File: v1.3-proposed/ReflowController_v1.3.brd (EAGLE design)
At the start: 95.2 x 50.8 mm, 52 parts, among them J1 AVR_SPI_PRG_62X3_LOCK

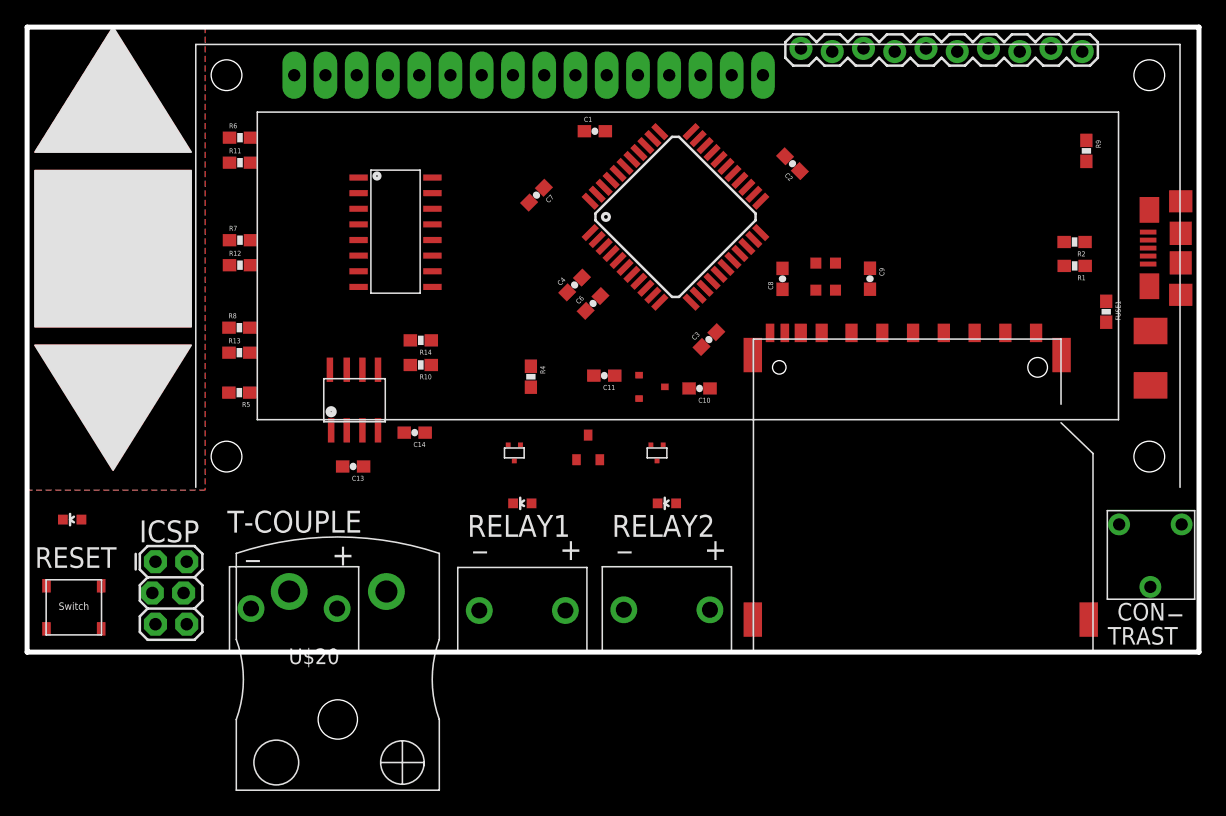
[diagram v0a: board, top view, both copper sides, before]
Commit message: Added 2 servo interfaces, many pin swaps
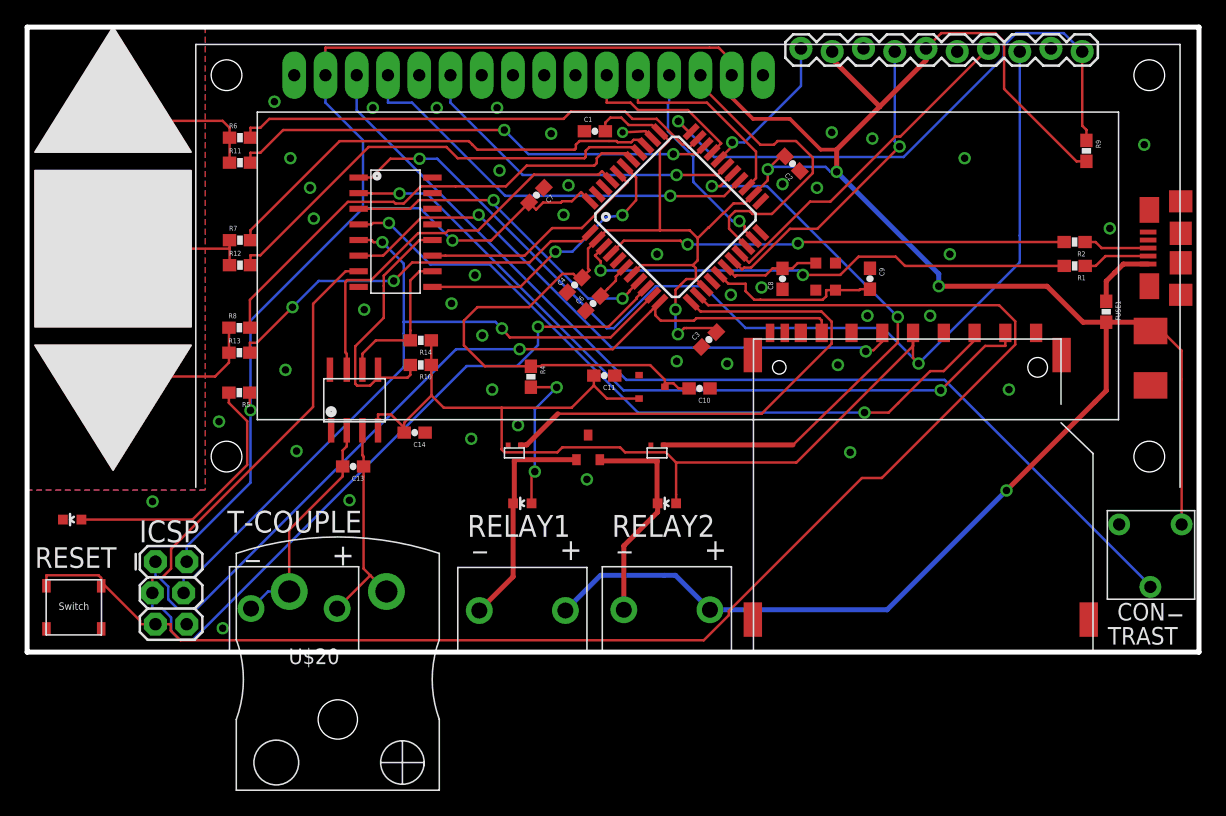
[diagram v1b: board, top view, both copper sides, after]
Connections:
- net D0: now also JP3.4; no longer U$16.GATE
- net D7: now also U$16.GATE; no longer JP3.4
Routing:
- net 5V: track 0.00 -> 362.2 mm, vias 0 -> 8
- net 3.3V: track 0.00 -> 164.8 mm, vias 0 -> 2
- net RESET: track 0.00 -> 121.5 mm
- net SCK: track 0.00 -> 90.0 mm, vias 0 -> 1
- net TRIM: track 0.00 -> 83.5 mm
- net MISO: track 0.00 -> 69.8 mm, vias 0 -> 1
- net SS-L: track 0.00 -> 61.8 mm, vias 0 -> 2
- net MOSI: track 0.00 -> 61.3 mm, vias 0 -> 2
- net MOSI-L: track 0.00 -> 59.5 mm, vias 0 -> 2
- net SCK-L: track 0.00 -> 49.6 mm, vias 0 -> 2
- net HWB: track 0.00 -> 48.1 mm, vias 0 -> 1
- net D7: track 0.00 -> 46.2 mm, vias 0 -> 2
- net B7: track 0.00 -> 42.6 mm
- net N$7: track 0.00 -> 41.2 mm, vias 0 -> 2
- net UPSENSE: track 0.00 -> 39.7 mm, vias 0 -> 2
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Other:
- board text added: "~3"
- board text removed: "~6"

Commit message: Added 2 servo interfaces, many pin swaps
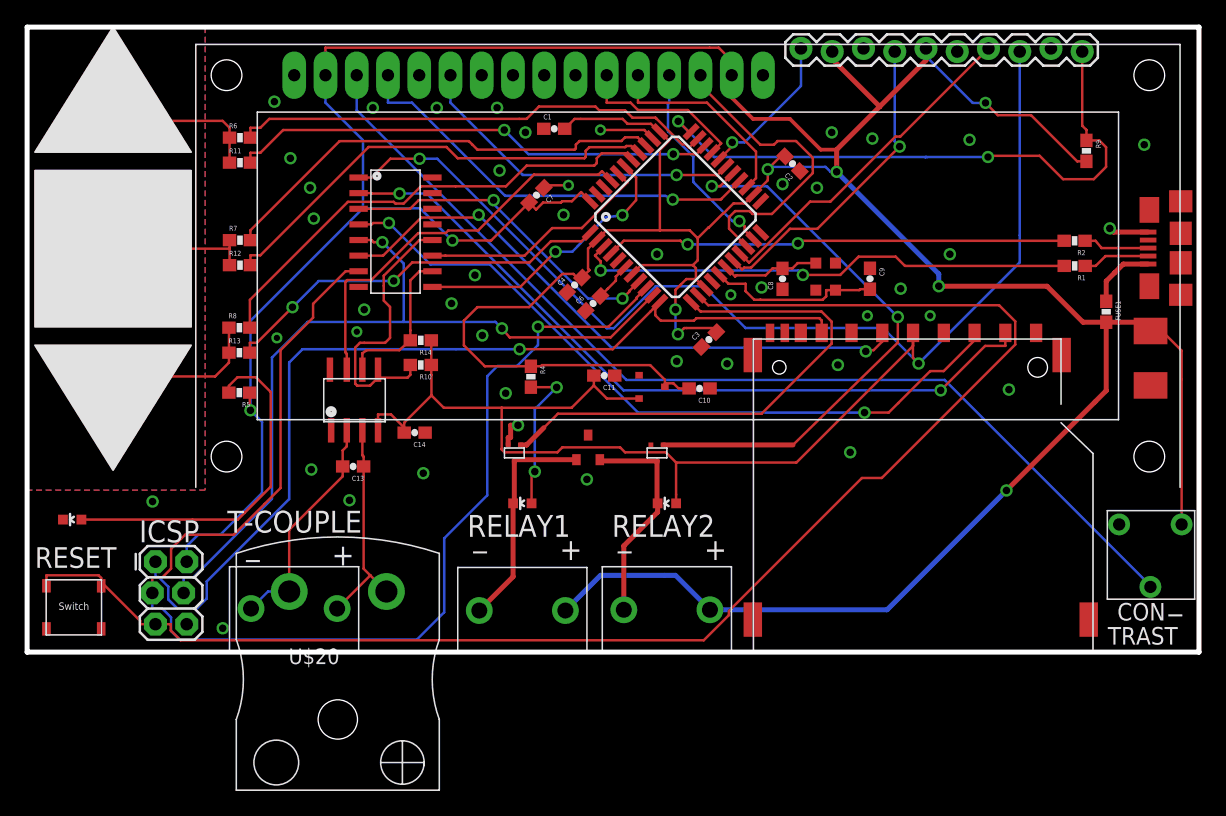
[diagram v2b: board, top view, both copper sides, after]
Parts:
- moved C1 3.31 mm to (42.8, 52.7)
- moved R2 0.10 mm to (85.1, 43.6)
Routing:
- net SCK: track 90.0 -> 101.5 mm
- net GND: track 2.72 -> 12.3 mm, vias 44 -> 45
- net MISO: track 69.8 -> 77.1 mm
- net N$4: track 21.8 -> 28.9 mm
- net MOSI: track 61.3 -> 65.9 mm
- net 5V: track 362.2 -> 363.8 mm, vias 8 -> 9
- net TC-SCK-L: track 21.3 -> 22.9 mm
- net HWB: track 48.1 -> 49.6 mm, vias 1 -> 2

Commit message: Added 2 servo interfaces, many pin swaps
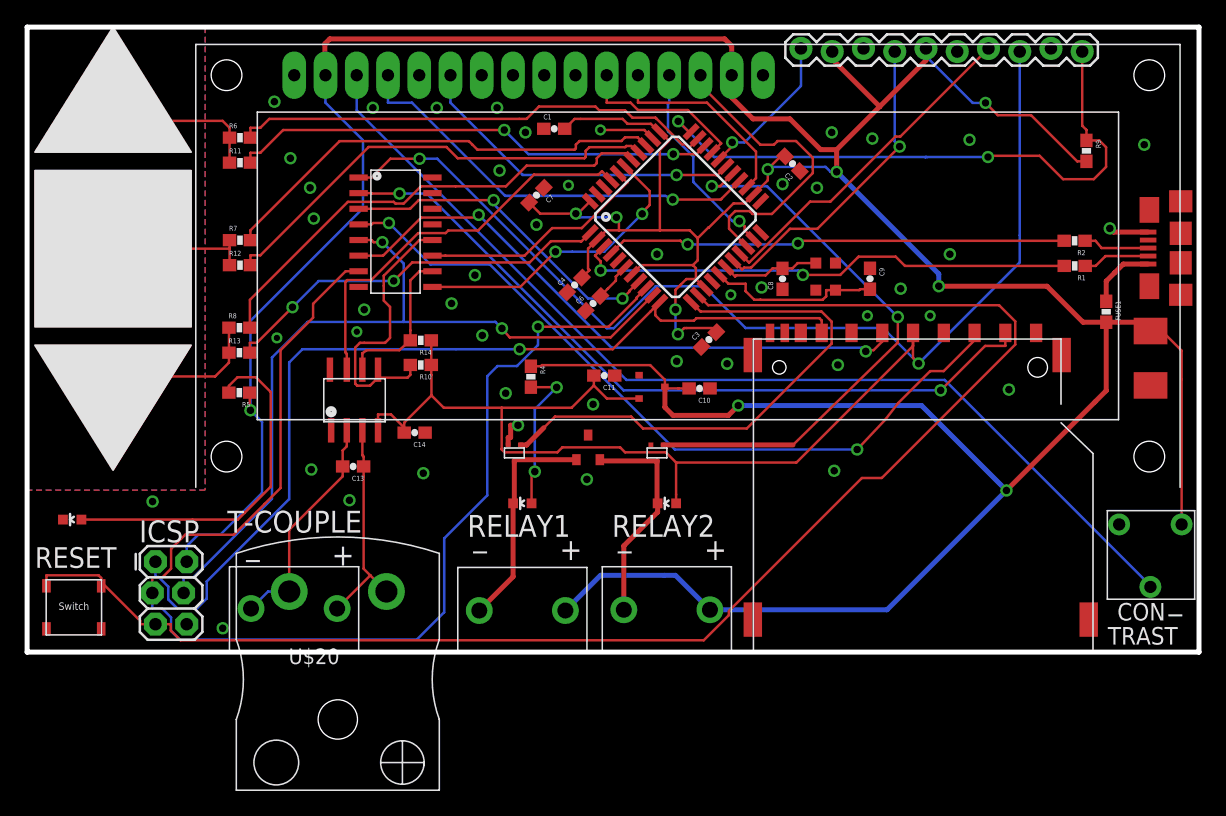
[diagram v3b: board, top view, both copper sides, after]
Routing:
- net 5V: track 363.8 -> 367.7 mm, vias 9 -> 11
- net MOSI-L: track 59.5 -> 62.2 mm
- net F4: track 22.6 -> 24.4 mm
- net GND: track 12.3 -> 10.5 mm, vias 45 -> 46
- net B7: track 42.6 -> 43.4 mm

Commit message: Added 2 servo interfaces, many optimizations
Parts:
- added R3: 390, SparkFun-Passives:0603-RES
- R4: value 150 -> 680
- R5: value 150 -> 510
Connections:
- new net N$6: LED3.A, R3.2
- net 3.3V: no longer LED3.A
- net 5V: now also R3.1
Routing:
- net 3.3V: track 164.8 -> 137.8 mm, vias 2 -> 3
- net 5V: track 367.7 -> 379.4 mm
- net N$6: track 0.00 -> 2.65 mm
- net GND: vias 46 -> 48
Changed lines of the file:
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@@
 <attribute name="VALUE" x="4.6785" y="22.0108" size="0.4064" layer="27" rot="R180"/>
 </element>
-<element name="R4" library="SparkFun-Passives" package="0603-RES" value="150" x="40.9472" y="32.5431" rot="R270"/>
-<element name="R5" library="SparkFun-Passives" package="0603-RES" value="150" x="17.25" y="31.25" rot="R180"/>
+<element name="R4" library="SparkFun-Passives" package="0603-RES" value="680" x="40.9472" y="32.5431" rot="R270"/>
+<element name="R5" library="SparkFun-Passives" package="0603-RES" value="510" x="17.25" y="31.25" rot="R180"/>
 <element name="U$13" library="JKCustom" package="CAPTOUCH_ARROW" value="CAPTOUCH_ARROW" x="6.985" y="50.8"/>
 <element name="U$14" library="JKCustom" package="CAPTOUCH_ARROW" value="CAPTOUCH_ARROW" x="6.985" y="35.1028" rot="R180"/>
@@
 <element name="JP3" library="SparkFun-Connectors" package="1X10_LOCK" value="M10LOCK" x="62.9" y="59.1" smashed="yes"/>
 <element name="R9" library="SparkFun-Passives" package="0603-RES" value="10K" x="86.1" y="50.9" rot="R270"/>
+<element name="R3" library="SparkFun-Passives" package="0603-RES" value="390" x="53.6" y="24.9" rot="R180"/>
 </elements>
 <signals>
@@
 <via x="59.7" y="39.8" extent="1-16" drill="0.609596875" diameter="1.016"/>
 <via x="76.6" y="51.8" extent="1-16" drill="0.609596875" diameter="1.016"/>
-<via x="65.6" y="24.9" extent="1-16" drill="0.609596875" diameter="1.016"/>
+<via x="62.7" y="22.5" extent="1-16" drill="0.609596875" diameter="1.016"/>
 <via x="90.8" y="51.4" extent="1-16" drill="0.609596875" diameter="1.016"/>
 <via x="71" y="39.7" extent="1-16" drill="0.609596875" diameter="1.016"/>
@@
 <via x="57.2" y="39.2" extent="1-16" drill="0.508" diameter="0.762"/>
 <via x="52.8" y="33.8" extent="1-16" drill="0.609596875" diameter="1.016"/>
-<via x="38.9" y="31.2" extent="1-16" drill="0.609596875" diameter="1.016"/>
+<via x="35.9" y="32.2" extent="1-16" drill="0.609596875" diameter="1.016"/>
 <via x="45.5" y="24.2" extent="1-16" drill="0.609596875" diameter="1.016"/>
 <via x="51.2" y="42.5" extent="1-16" drill="0.609596875" diameter="1.016"/>
@@
 <wire x1="39.3" y1="28.6" x2="39.9" y2="28.6" width="0.4064" layer="1"/>
 <via x="46" y="30.3" extent="1-16" drill="0.609596875" diameter="1.016"/>
+<via x="47.6" y="28.2" extent="1-16" drill="0.609596875" diameter="1.016"/>
+<via x="43.6" y="28.2" extent="1-16" drill="0.609596875" diameter="1.016"/>
 </signal>
 <signal name="5V">
@@
 <wire x1="40.80065625" y1="46.69955625" x2="41.7002125" y2="45.8" width="0.2032" layer="1"/>
 <wire x1="41.7002125" y1="45.8" x2="44.6" y2="45.8" width="0.2032" layer="1"/>
+<contactref element="R3" pad="1"/>
+<wire x1="54.45" y1="24.9" x2="55.5" y2="23.95" width="0.2032" layer="1"/>
+<wire x1="55.5" y1="23.95" x2="55.5" y2="13.6" width="0.2032" layer="1"/>
 <wire x1="61.6069" y1="50.4598" x2="61.60685625" y2="50.459840625" width="0" layer="19" extent="1-1"/>
 <wire x1="59.065959375" y1="47.372175" x2="59.066" y2="47.3722" width="0" layer="19" extent="1-1"/>
@@
 <contactref element="U$1" pad="8"/>
 <contactref element="U$8" pad="P$3"/>
-<wire x1="37.9142" y1="46.8963" x2="37.9142" y2="46.5858" width="0.2032" layer="16"/>
-<wire x1="37.9142" y1="46.5858" x2="45.5978" y2="38.9022" width="0.2032" layer="16"/>
 <wire x1="45.5978" y1="38.9022" x2="48.3917" y2="38.9022" width="0.2032" layer="16"/>
 <wire x1="27.9989" y1="46.194" x2="31.1303" y2="46.194" width="0.2032" layer="1"/>
@@
 <via x="48.3917" y="38.9022" extent="1-16" drill="0.609596875" diameter="1.016"/>
 <via x="37.9142" y="46.8963" extent="1-16" drill="0.609596875" diameter="1.016"/>
+<wire x1="45.5978" y1="38.9022" x2="44" y2="40.5" width="0.2032" layer="16"/>
+<wire x1="44" y1="40.5" x2="44" y2="41.1" width="0.2032" layer="16"/>
+<wire x1="44" y1="41.1" x2="43.4" y2="41.7" width="0.2032" layer="16"/>
+<wire x1="43.4" y1="41.7" x2="42.7" y2="41.7" width="0.2032" layer="16"/>
+<wire x1="37.9142" y1="46.8963" x2="38.1142" y2="46.2858" width="0.2032" layer="16"/>
+<wire x1="38.1142" y1="46.2858" x2="42.7" y2="41.7" width="0.2032" layer="16"/>
 <wire x1="49.7322" y1="40.3011" x2="49.73215" y2="40.301109375" width="0" layer="19" extent="1-1"/>
 </signal>
@@
 <contactref element="C14" pad="2"/>
 <contactref element="R14" pad="1"/>
-<contactref element="LED3" pad="A"/>
 <contactref element="R10" pad="1"/>
 <contactref element="JP3" pad="8"/>
 <wire x1="27.9989" y1="48.734" x2="29.5268" y2="50.2619" width="0.2032" layer="1"/>
 <wire x1="29.5268" y1="50.2619" x2="31.8966" y2="50.2619" width="0.2032" layer="1"/>
-<wire x1="47.1135" y1="36.4833" x2="33.335" y2="50.2618" width="0.2032" layer="16"/>
-<wire x1="33.335" y1="50.2618" x2="31.8966" y2="50.2618" width="0.2032" layer="16"/>
 <wire x1="31.8966" y1="50.2618" x2="31.8966" y2="50.2619" width="0.2032" layer="16"/>
-<wire x1="52.75" y1="25.5696" x2="52.75" y2="22.9549" width="0.2032" layer="1"/>
-<wire x1="72.0103" y1="35.0497" x2="62.5302" y2="25.5696" width="0.2032" layer="1"/>
-<wire x1="62.5302" y1="25.5696" x2="52.75" y2="25.5696" width="0.2032" layer="1"/>
+<wire x1="72.0103" y1="35.0497" x2="63.1302" y2="26.0696" width="0.2032" layer="1"/>
+<wire x1="63.1302" y1="26.0696" x2="52.35" y2="26.0696" width="0.2032" layer="1"/>
 <wire x1="38.572" y1="26.6851" x2="38.572" y2="30.0218" width="0.2032" layer="1"/>
 <wire x1="38.572" y1="30.0218" x2="33.8663" y2="30.0218" width="0.2032" layer="1"/>
@@
 <wire x1="32.85" y1="33.5" x2="32.85" y2="32.6951" width="0.2032" layer="1"/>
 <wire x1="32.85" y1="33.5" x2="32.85" y2="35.5" width="0.2032" layer="1"/>
-<wire x1="52.75" y1="22.25" x2="52.75" y2="22.9549" width="0.2032" layer="1"/>
 <wire x1="72.0103" y1="36.1046" x2="72.0103" y2="35.0497" width="0.2032" layer="1"/>
 <via x="72.4603" y="33.6165" extent="1-16" drill="0.609596875" diameter="1.016"/>
-<wire x1="47.1135" y1="36.4833" x2="47.6833" y2="36.4833" width="0.2032" layer="16"/>
-<wire x1="47.6833" y1="36.4833" x2="51.1" y2="39.9" width="0.2032" layer="16"/>
-<wire x1="51.1" y1="39.9" x2="55" y2="39.9" width="0.2032" layer="16"/>
-<wire x1="55" y1="39.9" x2="58.4" y2="36.5" width="0.2032" layer="16"/>
-<wire x1="58.4" y1="36.5" x2="69.0438" y2="36.5" width="0.2032" layer="16"/>
-<wire x1="70.4438" y1="35.633" x2="72.4603" y2="33.6165" width="0.2032" layer="16"/>
 <wire x1="72.0103" y1="36.1046" x2="72" y2="36.1046" width="0.2032" layer="1"/>
 <wire x1="72" y1="36.1046" x2="72" y2="35" width="0.2032" layer="1"/>
@@
 <wire x1="80.68" y1="44.0362" x2="80.68" y2="41.8362" width="0.2032" layer="16"/>
 <wire x1="80.68" y1="41.8362" x2="72.4603" y2="33.6165" width="0.2032" layer="16"/>
-<wire x1="70.4438" y1="35.633" x2="69.5768" y2="36.5" width="0.2032" layer="16"/>
-<wire x1="69.5768" y1="36.5" x2="69.0438" y2="36.5" width="0.2032" layer="16"/>
 <wire x1="38.572" y1="26.6851" x2="38.572" y2="26.628" width="0.2032" layer="1"/>
 <wire x1="38.572" y1="26.628" x2="38.8" y2="26.4" width="0.2032" layer="1"/>
@@
 <wire x1="48.2" y1="26.8" x2="48.6" y2="26.4" width="0.2032" layer="1"/>
 <wire x1="48.6" y1="26.4" x2="51.9196" y2="26.4" width="0.2032" layer="1"/>
-<wire x1="51.9196" y1="26.4" x2="52.75" y2="25.5696" width="0.2032" layer="1"/>
+<wire x1="51.9196" y1="26.4" x2="52.35" y2="26.0696" width="0.2032" layer="1"/>
+<wire x1="31.8966" y1="50.2618" x2="33.3382" y2="50.2618" width="0.2032" layer="16"/>
+<wire x1="33.3382" y1="50.2618" x2="42.8" y2="40.8" width="0.2032" layer="16"/>
+<via x="42.8" y="40.8" extent="1-16" drill="0.6"/>
+<wire x1="42.8" y1="40.8" x2="40.1" y2="38.1" width="0.2032" layer="1"/>
+<wire x1="40.1" y1="38.1" x2="36.4" y2="38.1" width="0.2032" layer="1"/>
+<wire x1="36.4" y1="38.1" x2="33.8" y2="35.5" width="0.2032" layer="1"/>
+<wire x1="33.8" y1="35.5" x2="32.85" y2="35.5" width="0.2032" layer="1"/>
 </signal>
 <signal name="SS-L">
@@
 <wire x1="36.4832" y1="45.479" x2="36.7056" y2="45.7014" width="0.2032" layer="1"/>
 <via x="68.1653" y="34.6068" extent="1-16" drill="0.609596875" diameter="1.016"/>
-<wire x1="36.7056" y1="45.7014" x2="47.5002" y2="34.9068" width="0.2032" layer="16"/>
 <via x="36.7056" y="45.7014" extent="1-16" drill="0.609596875" diameter="1.016"/>
 <wire x1="69.5103" y1="36.1046" x2="69.5103" y2="35.4103" width="0.2032" layer="1"/>
@@
 <wire x1="47.5002" y1="34.9068" x2="67.8653" y2="34.9068" width="0.2032" layer="16"/>
 <wire x1="67.8653" y1="34.9068" x2="68.1653" y2="34.6068" width="0.2032" layer="16"/>
+<wire x1="36.7056" y1="45.7014" x2="36.7056" y2="45.1944" width="0.2032" layer="16"/>
+<wire x1="36.7056" y1="45.1944" x2="46.5" y2="35.4" width="0.2032" layer="16"/>
+<wire x1="46.5" y1="35.4" x2="46.9932" y2="34.9068" width="0.2032" layer="16"/>
+<wire x1="46.9932" y1="34.9068" x2="47.5002" y2="34.9068" width="0.2032" layer="16"/>
 </signal>
 <signal name="TC-SS-L">
@@
 <wire x1="25.65" y1="25.25" x2="25.65" y2="26.5557" width="0.2032" layer="1"/>
 <wire x1="25.65" y1="26.5557" x2="25.9821" y2="26.8878" width="0.2032" layer="1"/>
-<wire x1="21.3035" y1="15.0856" x2="19.5856" y2="15.0856" width="0.2032" layer="16"/>
-<wire x1="19.5856" y1="15.0856" x2="18.2" y2="13.7" width="0.2032" layer="16"/>
+<wire x1="21.3035" y1="15.0856" x2="20.1856" y2="15.0856" width="0.2032" layer="1"/>
+<wire x1="20.1856" y1="15.0856" x2="19.1" y2="14" width="0.2032" layer="1"/>
+<wire x1="19.1" y1="14" x2="18.5" y2="14" width="0.2032" layer="1"/>
+<wire x1="18.5" y1="14" x2="18.2" y2="13.7" width="0.2032" layer="1"/>
 </signal>
 <signal name="TC+">
@@
 <wire x1="56.2375" y1="50.2006" x2="56.23753125" y2="50.200603125" width="0" layer="19" extent="1-1"/>
 </signal>
+<signal name="N$6">
+<contactref element="LED3" pad="A"/>
+<contactref element="R3" pad="2"/>
+<wire x1="52.75" y1="24.9" x2="52.75" y2="22.25" width="0.2032" layer="1"/>
+</signal>
 </signals>
